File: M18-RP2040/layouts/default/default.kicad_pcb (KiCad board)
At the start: 2 copper layers, 79.5 x 39.8 mm, 71 parts

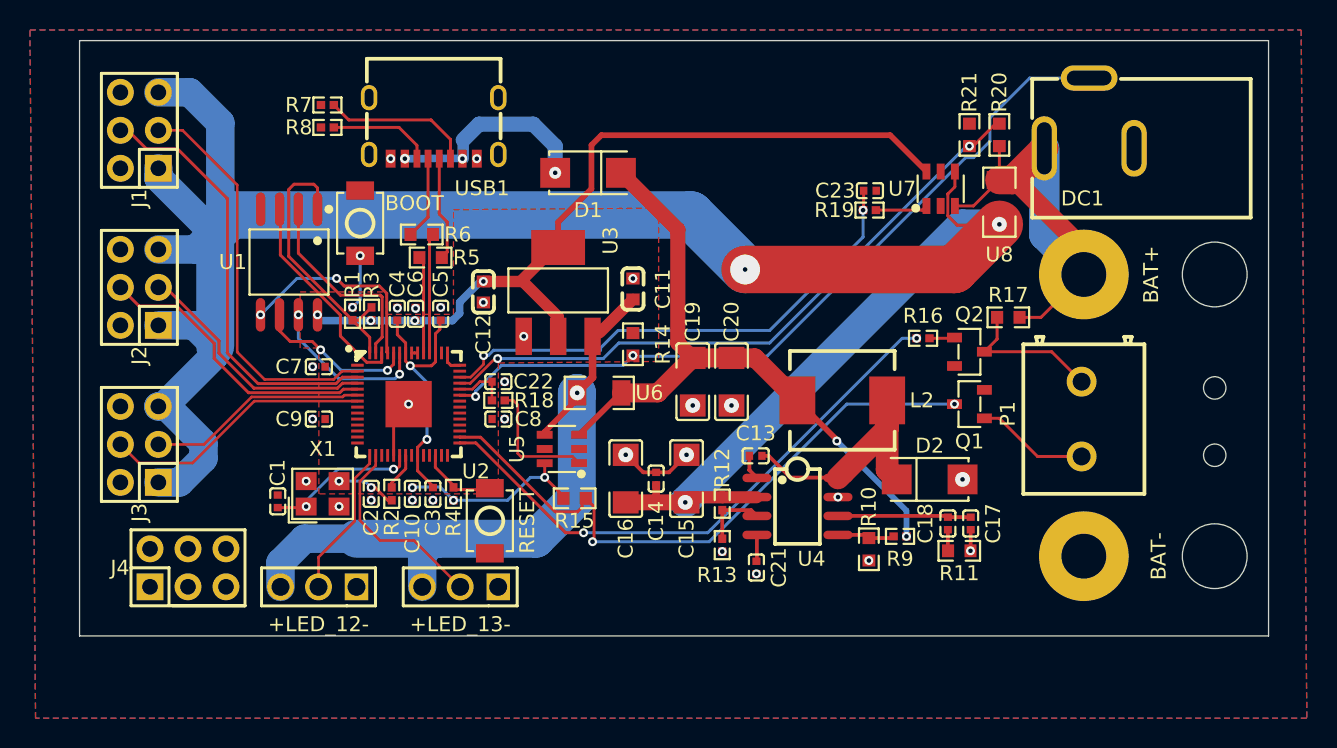
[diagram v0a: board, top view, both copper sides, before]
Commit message: Fixed USB port
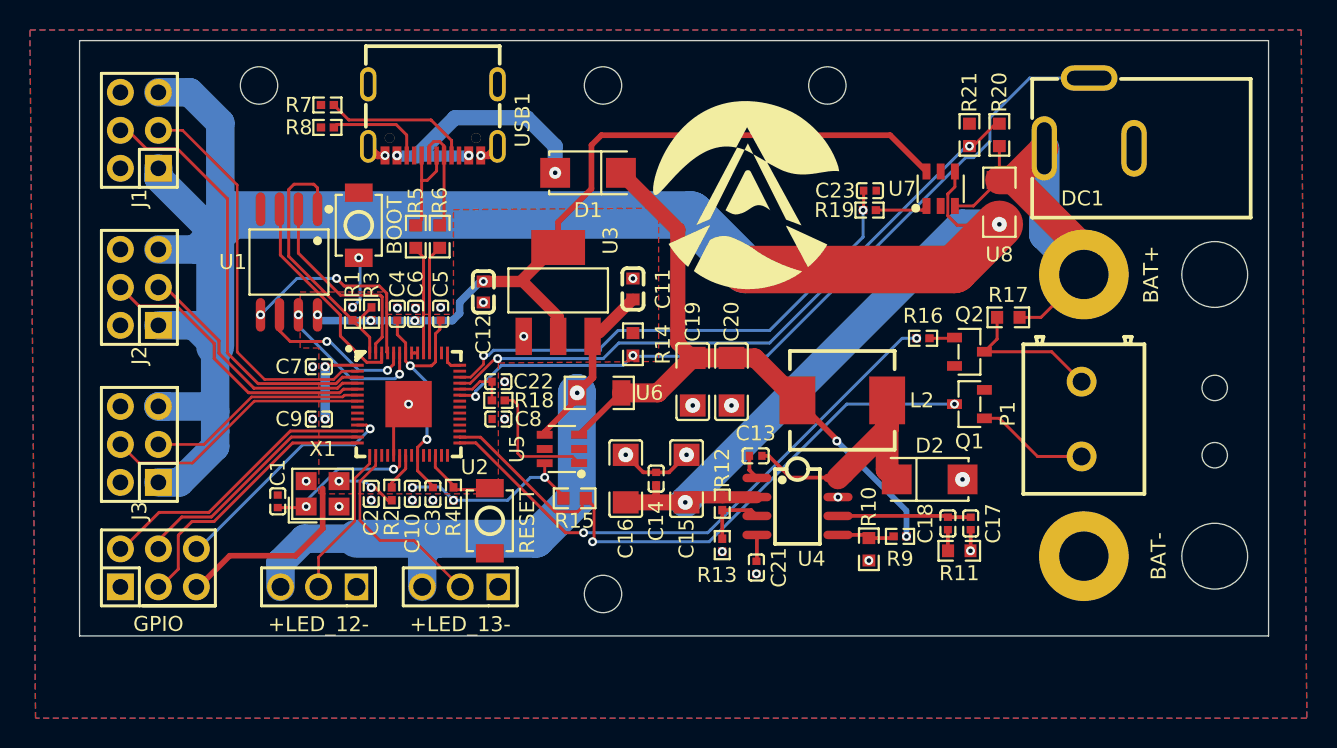
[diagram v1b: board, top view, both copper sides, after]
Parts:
- added QR*****: LED-GitHub-QR-MD, Silkscreen:LED-GitHub-QR-MD, B.Cu at (117.0, 129.4)
- added REF**: KiCad-Logo2_5mm_SilkScreen, Symbol:KiCad-Logo2_5mm_SilkScreen, B.Cu at (117.0, 119.7)
- added REF**: OSHW-Logo2_7.3x6mm_SilkScreen, Symbol:OSHW-Logo2_7.3x6mm_SilkScreen, B.Cu at (117.0, 111.7)
- C1, C2: value 22pF ±5% -> 20pF ±20%
- C10, C3, C4, C5, C6, C7, C8, C9: value 1µF ±10% -> 1µF ±20%
- C11: value 10µF ±10% -> 10µF ±20%
- C15, C16: value 4.7µF ±10% -> 4.7µF ±20%
- R1, R2: value 1kΩ ±1% -> 1kΩ ±5%
- R10: value 1.8kΩ ±1% -> {ℝ+}Ω
- R3, R4: value 10kΩ ±1% -> 10kΩ ±5%
- R5, R6: value 22Ω ±1% -> 22Ω ±5%
- R7, R8: value 5.1kΩ ±1% -> 5.1kΩ ±5%
- R9: value 10kΩ ±1% -> {ℝ+}Ω
- USB1: footprint Hanbo_Electronic_MC_403L68_Z20:USB-C-SMD_MC-403L68-Z20 -> BXCONN_UC09_0B16F00P11:USB-C_UC09-0B16F00P11
- moved GPIO 1.98 mm to (105.3, 135.3)
- moved R5 1.71 mm to (122.5, 113.1), turned to -90 degrees
- moved R6 1.21 mm to (124.1, 113.1), turned to -90 degrees
- moved USB1 0.56 mm to (123.6, 105.3)
- moved BOOT 0.17 mm to (118.7, 112.3)
- renumbered J4 to GPIO
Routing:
- net spi_cs: track 0.00 -> 19.0 mm
- net MOSI: track 0.00 -> 18.5 mm
- net 3V3: track 69.9 -> 88.2 mm, vias 7 -> 9
- net SCLK: track 0.00 -> 16.7 mm
- net MISO: track 0.00 -> 15.8 mm, vias 0 -> 1
- net vUSB: track 14.1 -> 17.5 mm
- net GND: track 10.3 -> 13.0 mm
- net DATA_N: track 5.55 -> 7.45 mm
- net V+: track 149.7 -> 151.2 mm
- net USB_DP: track 6.38 -> 7.35 mm
- net USB_DM: track 7.93 -> 7.41 mm
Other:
- outline, holes or cut-outs redrawn
- board text added: "M18 RP2040 LED Controller V1.0.0 - June 2026"

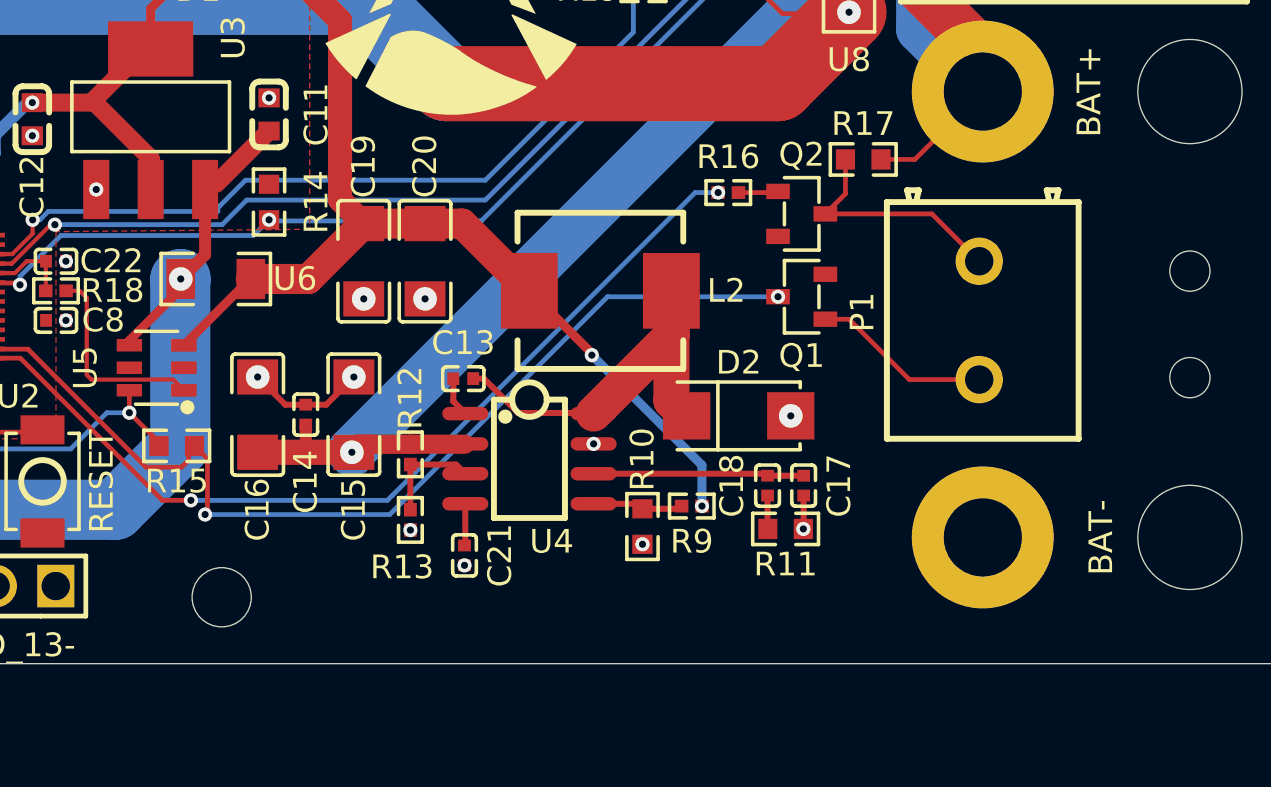
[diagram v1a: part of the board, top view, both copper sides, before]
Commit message: Added DC resistor divider
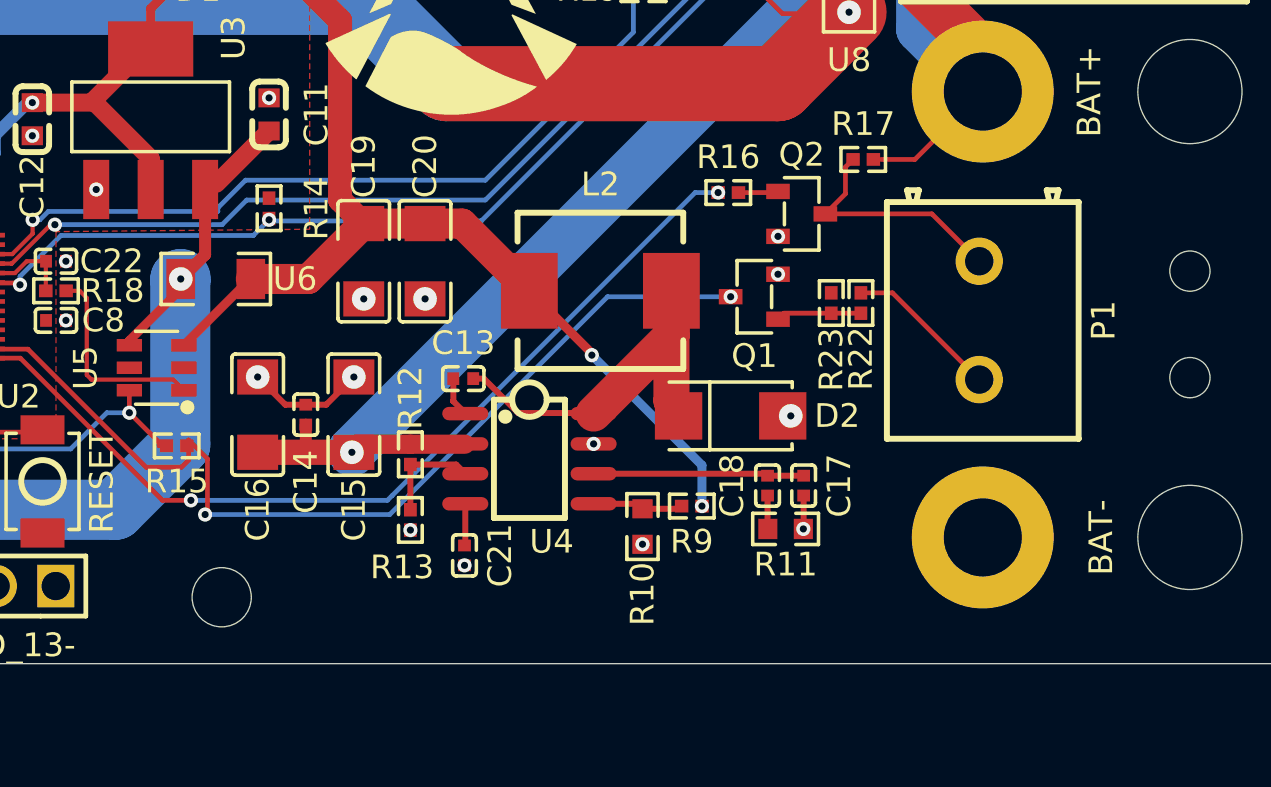
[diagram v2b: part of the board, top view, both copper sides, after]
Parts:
- removed QR*****: LED-GitHub-QR-MD, Silkscreen:LED-GitHub-QR-MD
- removed REF**: KiCad-Logo2_5mm_SilkScreen, Symbol:KiCad-Logo2_5mm_SilkScreen
- removed REF**: OSHW-Logo2_7.3x6mm_SilkScreen, Symbol:OSHW-Logo2_7.3x6mm_SilkScreen
- added R22: 10kΩ ±1%, UNI_ROYAL_0402WGF1002TCE:R0402, F.Cu at (162.0, 124.6)
- added R23: 10kΩ ±1%, UNI_ROYAL_0402WGF1002TCE:R0402, F.Cu at (160.8, 124.6)
- C1, C2: value 20pF ±20% -> 22pF ±5%
- C10, C3, C4, C5, C6, C7, C8, C9: value 1µF ±20% -> 1µF ±10%
- C11: value 10µF ±20% -> 10µF ±10%
- C15, C16: value 4.7µF ±20% -> 4.7µF ±10%
- R1, R2: value 1kΩ ±5% -> 1kΩ ±1%
- R10: value {ℝ+}Ω -> 1.8kΩ ±1%
- R14, R15, R17: footprint UNI_ROYAL_0603WAF1002T5E:R0603 -> UNI_ROYAL_0402WGF1002TCE:R0402
- R3, R4: value 10kΩ ±5% -> 10kΩ ±1%
- R5, R6: value 22Ω ±5% -> 22Ω ±1%
- R7, R8: value 5.1kΩ ±5% -> 5.1kΩ ±1%
- R9: value {ℝ+}Ω -> 10kΩ ±1%
- moved Q1 2.00 mm to (157.5, 124.3)
- moved D2 0.34 mm to (156.5, 129.3)
- moved R14 0.27 mm to (137.0, 120.6)
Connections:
- net GPI54 renamed GPIO5
- Q1 pad 1: DC -> G
- Q2 pad 1: G -> G-1
- R16 pad 1: G -> G-1
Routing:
- net D: track 42.8 -> 40.8 mm
- net G: track 1.69 -> 3.61 mm
- net G-1: track 0.00 -> 1.69 mm
- net DC: track 7.56 -> 6.52 mm
- net GND: vias 28 -> 30

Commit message: Re-added m18 rp2040 logos
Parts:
- added QR*****: LED-GitHub-QR-MD, Silkscreen:LED-GitHub-QR-MD, B.Cu at (124.0, 115.2)
- added REF**: KiCad-Logo2_5mm_SilkScreen, Symbol:KiCad-Logo2_5mm_SilkScreen, B.Cu at (128.5, 124.2)
- added REF**: OSHW-Logo2_7.3x6mm_SilkScreen, Symbol:OSHW-Logo2_7.3x6mm_SilkScreen, B.Cu at (117.5, 124.2)
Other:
- board text added: "M18 RP2040 LED Controller V1.0.1 - June 2026"
- board text removed: "M18 RP2040 LED Controller V1.0.0 - June 2026"
